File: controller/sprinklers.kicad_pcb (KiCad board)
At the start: 2 copper layers, 155.1 x 162.1 mm, 144 parts, among them J1 Conn_01x02, J2 Conn_01x02, J3 Conn_01x02, J4 Conn_01x02, J5 Conn_01x02, J6 Conn_01x02, K1 SANYOU_SRD_Form_C, K2 SANYOU_SRD_Form_C, K3 SANYOU_SRD_Form_C, K4 SANYOU_SRD_Form_C, K5 SANYOU_SRD_Form_C, K6 SANYOU_SRD_Form_C, Q1 Q_NMOS_GDS, Q2 Q_NMOS_GDS, Q3 Q_NMOS_GDS, Q4 Q_NMOS_GDS, Q5 Q_NMOS_GDS, Q6 Q_NMOS_GDS, U1 LM2596S-5, U2 ESP32-WROOM-32U, U3 AP1117-33

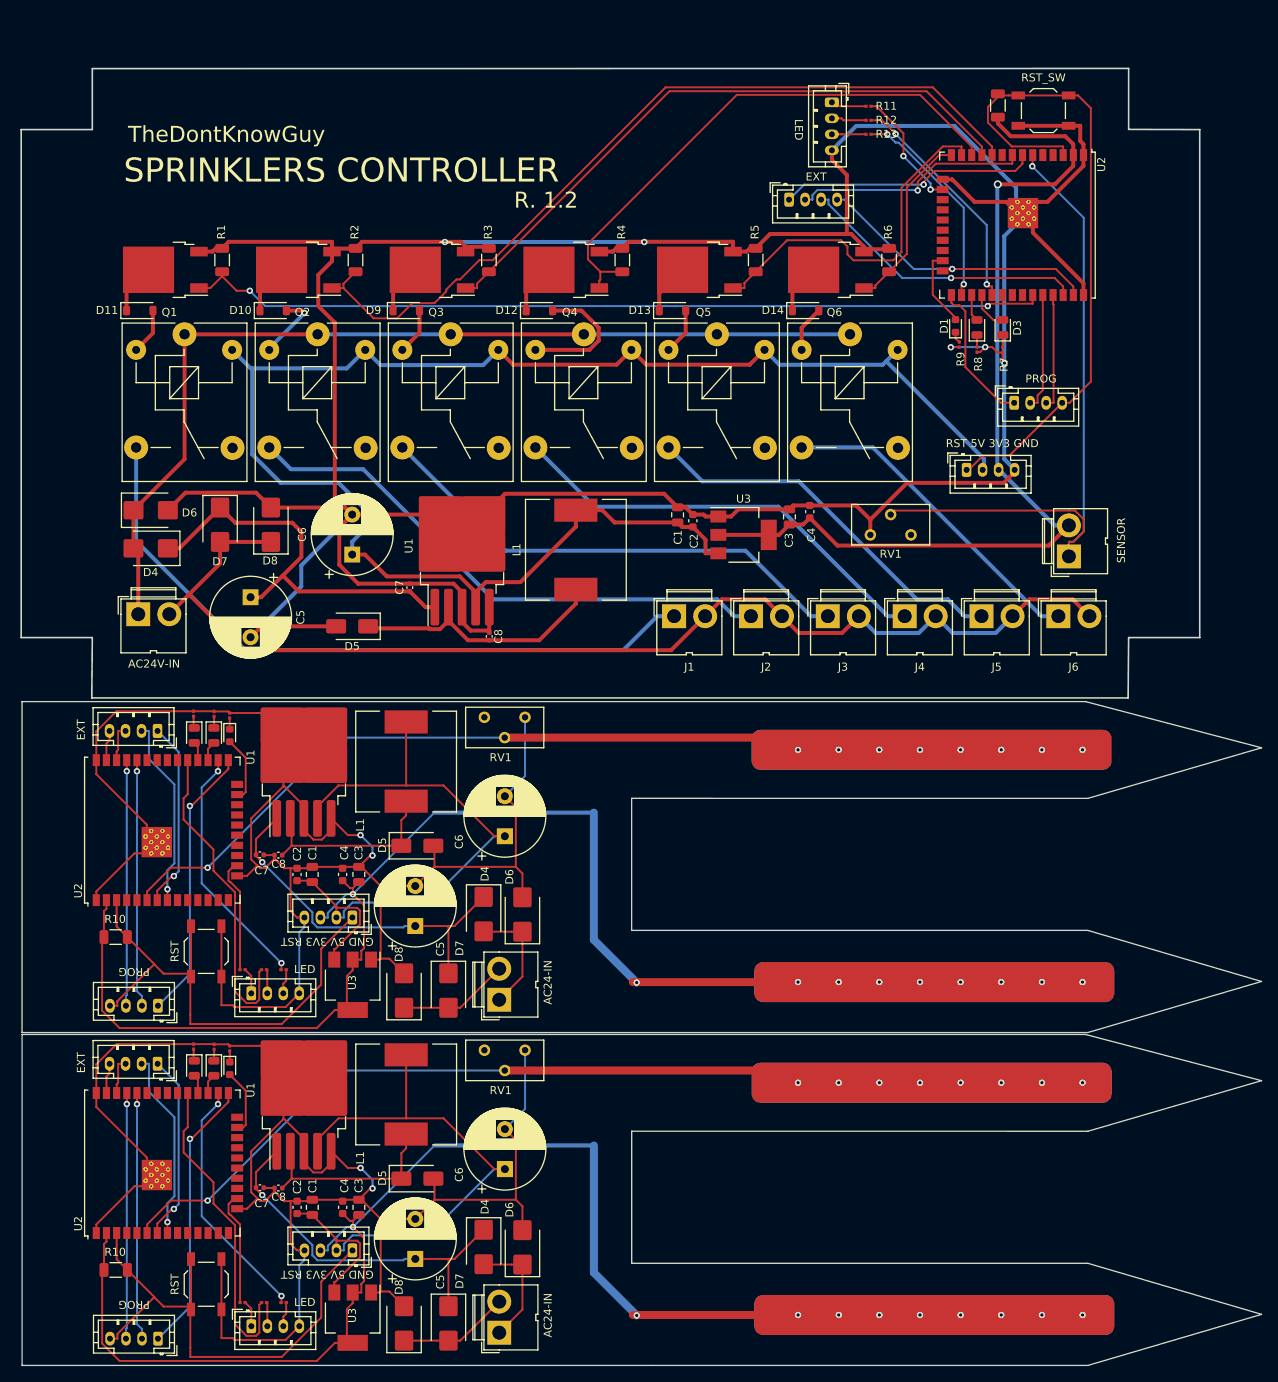
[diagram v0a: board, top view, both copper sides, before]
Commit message: fix footprint
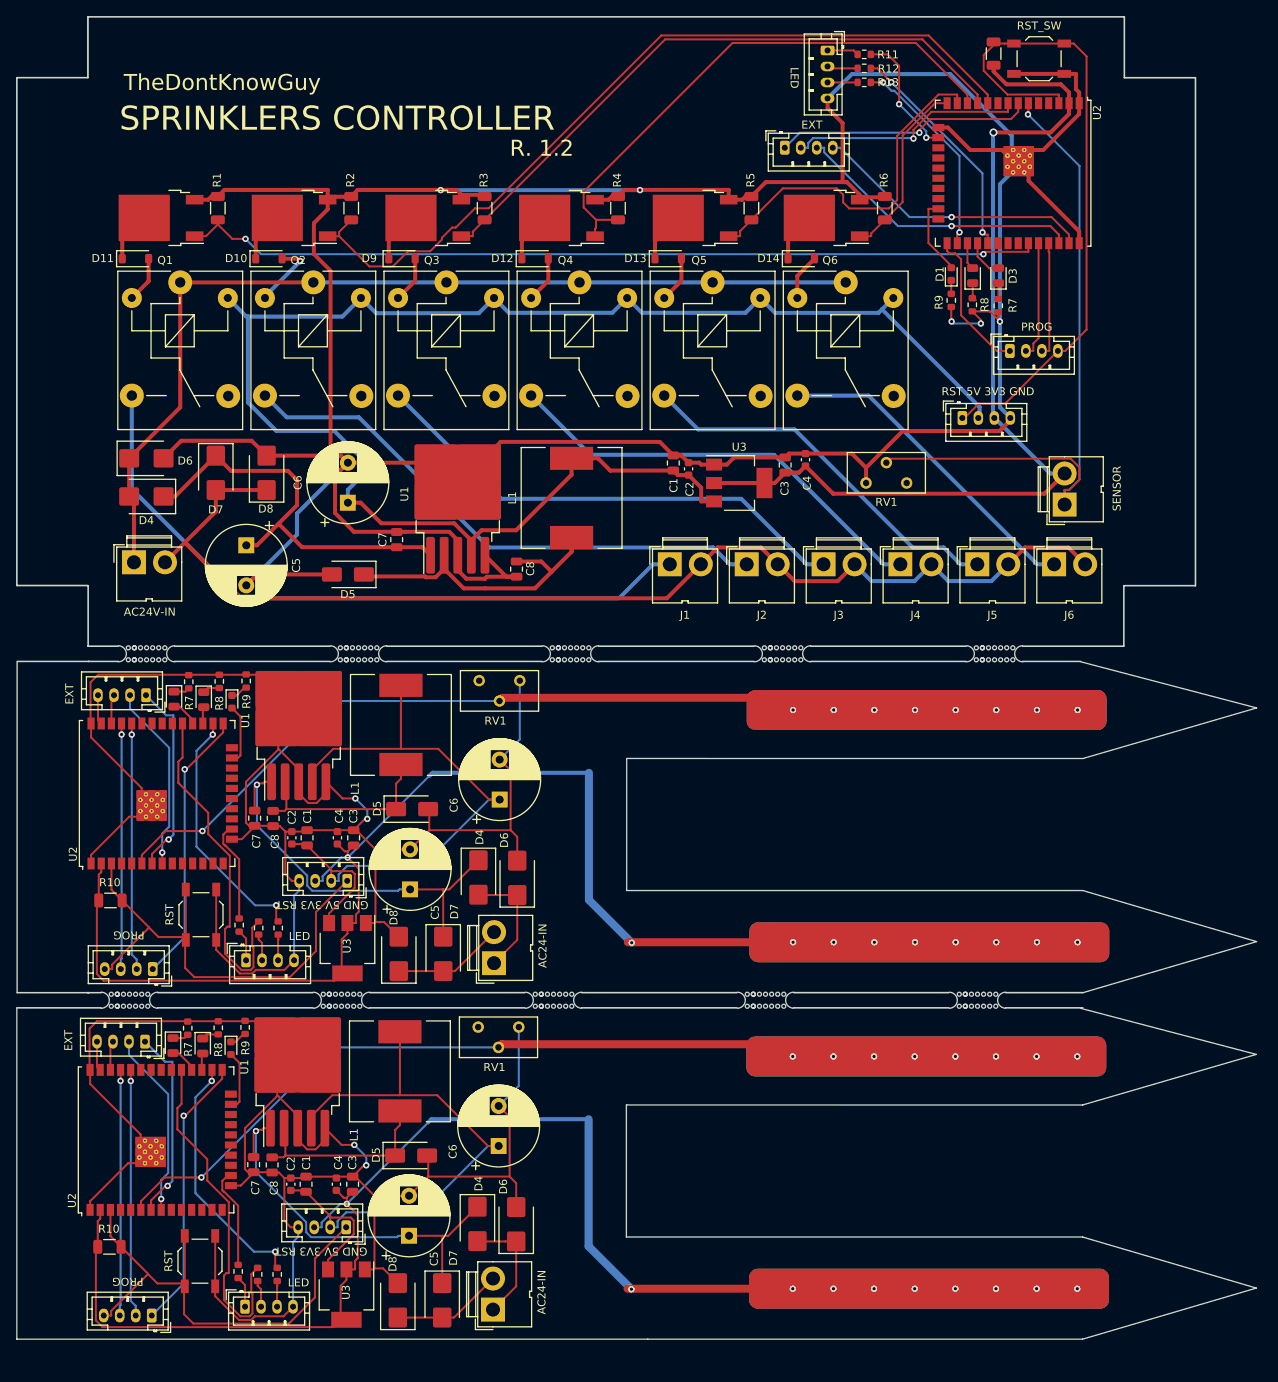
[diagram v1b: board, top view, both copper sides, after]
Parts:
- removed the ? at (129.9, 175.0) (x2)
- removed the ? at (31.8, 162.4)
- removed the ? at (129.6, 145.9) (x2)
- removed the ? at (86.4, 35.6)
- removed the AC24-IN1 at (30.4, 87.4)
- removed the AC24-IN1 at (75.5, 135.6)
- removed the AC24-IN1 at (75.5, 177.2)
- removed the C1 at (52.2, 119.9)
- removed the C1 at (52.2, 161.5)
- removed the C1 at (97.8, 75.0)
- removed the C2 at (99.7, 75.7)
- removed the C2 at (50.3, 119.9)
- removed the C2 at (50.3, 161.5)
- removed the C3 at (111.8, 75.2)
- removed the C3 at (58.0, 119.9)
- removed the C3 at (58.0, 161.5)
- removed the C4 at (56.0, 119.9)
- removed the C4 at (114.3, 74.6)
- removed the C4 at (56.0, 161.5)
- removed the C5 at (44.5, 85.3)
- removed the C5 at (65.0, 126.4)
- removed the C5 at (65.0, 168.0)
- removed the C6 at (57.1, 79.9)
- removed the C6 at (76.2, 115.1)
- removed the C6 at (76.2, 156.7)
- removed the C7 at (45.6, 159.1)
- removed the C7 at (64.4, 84.1)
- removed the C7 at (45.6, 117.5)
- removed the C8 at (47.9, 159.1)
- removed the C8 at (47.9, 117.5)
- removed the C8 at (74.3, 90.2)
- removed the D1 at (132.6, 51.4)
- removed the D1 at (41.8, 102.5)
- removed the D1 at (41.8, 144.1)
- removed the D2 at (135.3, 51.5)
- removed the D2 at (39.9, 144.1)
- removed the D2 at (39.9, 102.5)
- removed the D3 at (138.5, 51.5)
- removed the D3 at (37.4, 102.5)
- removed the D3 at (37.4, 144.1)
- removed the D4 at (73.6, 166.5)
- removed the D4 at (73.6, 124.9)
- removed the D4 at (32.0, 79.2)
- removed the D5 at (65.3, 157.9)
- removed the D5 at (57.1, 88.9)
- removed the D5 at (65.3, 116.3)
- removed the D6 at (32.0, 74.4)
- removed the D6 at (78.4, 124.9)
- removed the D6 at (78.4, 166.5)
- removed the D7 at (69.2, 134.4)
- removed the D7 at (40.6, 76.2)
- removed the D7 at (69.2, 176.0)
- removed the D8 at (63.6, 134.4)
- removed the D8 at (63.6, 176.0)
- removed the D8 at (47.0, 76.2)
- removed the EXT1 at (32.8, 102.0)
- removed the EXT1 at (32.8, 143.6)
- removed the EXT1 at (111.8, 35.6)
- removed the L1 at (63.9, 105.8)
- removed the L1 at (63.9, 147.4)
- removed the L1 at (85.1, 79.3)
- removed the LED1 at (44.5, 176.4)
- removed the LED1 at (117.1, 23.4)
- removed the LED1 at (44.5, 134.8)
- removed the POWER1 at (57.2, 125.3)
- removed the POWER1 at (134.0, 69.3)
- removed the POWER1 at (57.2, 166.9)
- removed the PROG1 at (32.9, 177.9)
- removed the PROG1 at (32.9, 136.3)
- removed the PROG1 at (139.9, 61.0)
- removed the R10 at (27.6, 127.7)
- removed the R10 at (137.9, 23.8)
- removed the R10 at (27.6, 169.4)
- removed the R11 at (43.5, 173.4)
- removed the R11 at (121.7, 23.9)
- removed the R11 at (43.4, 131.8)
- removed the R12 at (46.1, 131.8)
- removed the R12 at (46.1, 173.4)
- removed the R12 at (121.7, 25.6)
- removed the R13 at (48.6, 173.4)
- removed the R13 at (48.6, 131.8)
- removed the R13 at (121.7, 27.4)
- removed the R7 at (37.3, 141.4)
- removed the R7 at (138.5, 54.4)
- removed the R7 at (37.3, 99.8)
- removed the R8 at (39.9, 141.5)
- removed the R8 at (39.9, 99.9)
- removed the R8 at (135.2, 54.3)
- removed the R9 at (133.0, 53.7)
- removed the R9 at (41.8, 141.7)
- removed the R9 at (41.8, 100.1)
- removed the RST_SW1 at (38.9, 171.1)
- removed the RST_SW1 at (143.6, 24.4)
- removed the RST_SW1 at (38.9, 129.5)
- removed the RV1 at (121.9, 77.5)
- removed the RV1 at (78.8, 141.9)
- removed the RV1 at (78.8, 100.3)
- removed the U1 at (70.9, 78.9)
- removed the U1 at (51.1, 146.9)
- removed the U1 at (51.1, 105.3)
- removed the U2 at (33.4, 114.4)
- removed the U2 at (140.3, 38.7)
- removed the U2 at (33.4, 156.0)
- removed the U3 at (106.1, 77.5)
- removed the U3 at (57.2, 175.3)
- removed the U3 at (57.2, 133.7)
- added ? (x2): , , F.Cu at (128.9, 142.7)
- added ?: LOGO, my lib:sprinklers qr code, B.Cu at (85.8, 29.1)
- added ? (x2): , , F.Cu at (129.3, 171.7)
- added ?: LOGO, my lib:sprinklers qr code, B.Cu at (31.7, 163.6)
- added AC24-IN1: Conn_01x02, Connector:JWT_A3963_1x02_P3.96mm_Vertical, F.Cu at (74.8, 174.3)
- added AC24-IN1: Conn_01x02, Connector:JWT_A3963_1x02_P3.96mm_Vertical, F.Cu at (74.9, 131.0)
- added AC24-IN1: Conn_01x02, Connector:JWT_A3963_1x02_P3.96mm_Vertical, F.Cu at (29.9, 80.9)
- added C1: 10uF, Capacitor_SMD:C_0805_2012Metric, F.Cu at (51.4, 158.6)
- added C1: 10uF, Capacitor_SMD:C_0805_2012Metric, F.Cu at (51.5, 115.3)
- added C1: 10uF, Capacitor_SMD:C_0805_2012Metric, F.Cu at (97.3, 68.5)
- added C2: 100nF, Capacitor_SMD:C_0603_1608Metric, F.Cu at (49.6, 115.3)
- added C2: 100nF, Capacitor_SMD:C_0603_1608Metric, F.Cu at (49.5, 158.6)
- added C2: 100nF, Capacitor_SMD:C_0603_1608Metric, F.Cu at (99.2, 69.2)
- added C3: 10uF, Capacitor_SMD:C_0805_2012Metric, F.Cu at (111.3, 68.7)
- added C3: 10uF, Capacitor_SMD:C_0805_2012Metric, F.Cu at (57.3, 115.3)
- added C3: 10uF, Capacitor_SMD:C_0805_2012Metric, F.Cu at (57.2, 158.6)
- added C4: 100nF, Capacitor_SMD:C_0603_1608Metric, F.Cu at (113.8, 68.1)
- added C4: 100nF, Capacitor_SMD:C_0603_1608Metric, F.Cu at (55.3, 115.3)
- added C4: 100nF, Capacitor_SMD:C_0603_1608Metric, F.Cu at (55.2, 158.6)
- added C5: C_Polarized, Capacitor_THT:CP_Radial_D10.0mm_P5.00mm, F.Cu at (64.3, 165.1)
- added C5: C_Polarized, Capacitor_THT:CP_Radial_D10.0mm_P5.00mm, F.Cu at (64.4, 121.8)
- added C5: C_Polarized, Capacitor_THT:CP_Radial_D10.0mm_P5.00mm, F.Cu at (43.9, 78.8)
- added C6: C_Polarized, Capacitor_THT:CP_Radial_D10.0mm_P5.00mm, F.Cu at (75.6, 110.6)
- added C6: C_Polarized, Capacitor_THT:CP_Radial_D10.0mm_P5.00mm, F.Cu at (75.5, 153.9)
- added C6: C_Polarized, Capacitor_THT:CP_Radial_D10.0mm_P5.00mm, F.Cu at (56.6, 73.4)
- added C7: 25V 1uF X5R ±10% 0402 Multilayer Ceramic Capacitors MLCC - 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, Capacitor_SMD:C_0805_2012Metric, F.Cu at (44.8, 156.2)
- added C7: 25V 1uF X5R ±10% 0402 Multilayer Ceramic Capacitors MLCC - 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, Capacitor_SMD:C_0805_2012Metric, F.Cu at (62.7, 78.1)
- added C7: 25V 1uF X5R ±10% 0402 Multilayer Ceramic Capacitors MLCC - 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, Capacitor_SMD:C_0805_2012Metric, F.Cu at (45.0, 112.9)
- added C8: 25V 1uF X5R ±10% 0402 Multilayer Ceramic Capacitors MLCC - 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, Capacitor_SMD:C_0805_2012Metric, F.Cu at (47.3, 112.9)
- added C8: 25V 1uF X5R ±10% 0402 Multilayer Ceramic Capacitors MLCC - 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, Capacitor_SMD:C_0805_2012Metric, F.Cu at (77.7, 81.7)
- added C8: 25V 1uF X5R ±10% 0402 Multilayer Ceramic Capacitors MLCC - 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, Capacitor_SMD:C_0805_2012Metric, F.Cu at (47.1, 156.2)
- added D1: LED, LED_SMD:LED_0603_1608Metric, F.Cu at (132.0, 44.9)
- added D1: LED, LED_SMD:LED_0603_1608Metric, F.Cu at (42.0, 141.6)
- added D1: LED, LED_SMD:LED_0603_1608Metric, F.Cu at (42.1, 98.3)
- added D2: LED, LED_SMD:LED_0805_2012Metric, F.Cu at (38.5, 141.4)
- added D2: LED, LED_SMD:LED_0805_2012Metric, F.Cu at (38.6, 98.1)
- added D2: LED, LED_SMD:LED_0805_2012Metric, F.Cu at (134.7, 45.1)
- added D3: LED, LED_SMD:LED_0805_2012Metric, F.Cu at (137.9, 45.1)
- added D3: LED, LED_SMD:LED_0805_2012Metric, F.Cu at (34.8, 141.3)
- added D3: LED, LED_SMD:LED_0805_2012Metric, F.Cu at (34.9, 98.0)
- added D4: 900mV@2A 30ns 2A 50V DO-214AA Diodes, Diode_SMD:D_SMB, F.Cu at (31.4, 72.7)
- added D4: 900mV@2A 30ns 2A 50V DO-214AA Diodes, Diode_SMD:D_SMB, F.Cu at (72.9, 120.3)
- added D4: 900mV@2A 30ns 2A 50V DO-214AA Diodes, Diode_SMD:D_SMB, F.Cu at (72.8, 163.6)
- added D5: B140-E3, Diode_SMD:D_SMA, F.Cu at (64.6, 111.7)
- added D5: B140-E3, Diode_SMD:D_SMA, F.Cu at (64.5, 155.1)
- added D5: B140-E3, Diode_SMD:D_SMA, F.Cu at (56.6, 82.4)
- added D6: 900mV@2A 30ns 2A 50V DO-214AA Diodes, Diode_SMD:D_SMB, F.Cu at (31.4, 67.9)
- added D6: 900mV@2A 30ns 2A 50V DO-214AA Diodes, Diode_SMD:D_SMB, F.Cu at (77.7, 163.6)
- added D6: 900mV@2A 30ns 2A 50V DO-214AA Diodes, Diode_SMD:D_SMB, F.Cu at (77.8, 120.3)
- added D7: 900mV@2A 30ns 2A 50V DO-214AA Diodes, Diode_SMD:D_SMB, F.Cu at (68.4, 173.1)
- added D7: 900mV@2A 30ns 2A 50V DO-214AA Diodes, Diode_SMD:D_SMB, F.Cu at (68.5, 129.8)
- added D7: 900mV@2A 30ns 2A 50V DO-214AA Diodes, Diode_SMD:D_SMB, F.Cu at (40.1, 69.7)
- added D8: 900mV@2A 30ns 2A 50V DO-214AA Diodes, Diode_SMD:D_SMB, F.Cu at (62.9, 173.1)
- added D8: 900mV@2A 30ns 2A 50V DO-214AA Diodes, Diode_SMD:D_SMB, F.Cu at (46.5, 69.7)
- added D8: 900mV@2A 30ns 2A 50V DO-214AA Diodes, Diode_SMD:D_SMB, F.Cu at (63.0, 129.8)
- added EXT1: Conn_01x04_Pin, Connector_JST:JST_PH_B4B-PH-K_1x04_P2.00mm_Vertical, F.Cu at (31.3, 140.8)
- added EXT1: Conn_01x04_Pin, Connector_JST:JST_PH_B4B-PH-K_1x04_P2.00mm_Vertical, F.Cu at (31.4, 97.5)
- added EXT1: Conn_01x04_Pin, Connector_JST:JST_PH_B4B-PH-K_1x04_P2.00mm_Vertical, F.Cu at (111.2, 29.1)
- added L1: L, Inductor_SMD:L_12x12mm_H8mm, F.Cu at (63.1, 144.5)
- added L1: L, Inductor_SMD:L_12x12mm_H8mm, F.Cu at (84.6, 72.8)
- added L1: L, Inductor_SMD:L_12x12mm_H8mm, F.Cu at (63.2, 101.2)
- added LED1: Conn_01x04_Pin, Connector_JST:JST_PH_B4B-PH-K_1x04_P2.00mm_Vertical, F.Cu at (43.9, 130.6)
- added LED1: Conn_01x04_Pin, Connector_JST:JST_PH_B4B-PH-K_1x04_P2.00mm_Vertical, F.Cu at (43.8, 173.9)
- added LED1: Conn_01x04_Pin, Connector_JST:JST_PH_B4B-PH-K_1x04_P2.00mm_Vertical, F.Cu at (116.6, 16.9)
- added POWER1: Conn_01x04_Pin, Connector_JST:JST_PH_B4B-PH-K_1x04_P2.00mm_Vertical, F.Cu at (56.4, 164.0)
- added POWER1: Conn_01x04_Pin, Connector_JST:JST_PH_B4B-PH-K_1x04_P2.00mm_Vertical, F.Cu at (133.4, 62.9)
- added POWER1: Conn_01x04_Pin, Connector_JST:JST_PH_B4B-PH-K_1x04_P2.00mm_Vertical, F.Cu at (56.5, 120.7)
- added PROG1: Conn_01x04_Pin, Connector_JST:JST_PH_B4B-PH-K_1x04_P2.00mm_Vertical, F.Cu at (32.2, 131.7)
- added PROG1: Conn_01x04_Pin, Connector_JST:JST_PH_B4B-PH-K_1x04_P2.00mm_Vertical, F.Cu at (139.4, 54.5)
- added PROG1: Conn_01x04_Pin, Connector_JST:JST_PH_B4B-PH-K_1x04_P2.00mm_Vertical, F.Cu at (32.1, 175.0)
- added R10: 10K, Resistor_SMD:R_1206_3216Metric, F.Cu at (26.9, 123.2)
- added R10: 10K, Resistor_SMD:R_1206_3216Metric, F.Cu at (26.8, 166.5)
- added R10: 10K, Resistor_SMD:R_1206_3216Metric, F.Cu at (137.3, 17.3)
- added R11: 130, Resistor_SMD:R_0603_1608Metric, F.Cu at (121.2, 17.4)
- added R11: 130, Resistor_SMD:R_0603_1608Metric, F.Cu at (43.0, 126.2)
- added R11: 130, Resistor_SMD:R_0603_1608Metric, F.Cu at (42.9, 169.5)
- added R12: 130, Resistor_SMD:R_0603_1608Metric, F.Cu at (45.3, 169.9)
- added R12: 130, Resistor_SMD:R_0603_1608Metric, F.Cu at (45.5, 126.6)
- added R12: 130, Resistor_SMD:R_0603_1608Metric, F.Cu at (121.2, 19.2)
- added R13: 130, Resistor_SMD:R_0603_1608Metric, F.Cu at (47.9, 126.6)
- added R13: 130, Resistor_SMD:R_0603_1608Metric, F.Cu at (47.8, 169.9)
- added R13: 130, Resistor_SMD:R_0603_1608Metric, F.Cu at (121.2, 20.9)
- added R7: 130, Resistor_SMD:R_0603_1608Metric, F.Cu at (36.6, 139.1)
- added R7: 130, Resistor_SMD:R_0603_1608Metric, F.Cu at (137.9, 48.8)
- added R7: 130, Resistor_SMD:R_0603_1608Metric, F.Cu at (36.7, 95.8)
- added R8: 130, Resistor_SMD:R_0603_1608Metric, F.Cu at (40.5, 95.8)
- added R8: 130, Resistor_SMD:R_0603_1608Metric, F.Cu at (134.7, 48.7)
- added R8: 130, Resistor_SMD:R_0603_1608Metric, F.Cu at (40.4, 139.1)
- added R9: 130, Resistor_SMD:R_0603_1608Metric, F.Cu at (43.8, 139.0)
- added R9: 130, Resistor_SMD:R_0603_1608Metric, F.Cu at (43.9, 95.7)
- added R9: 130, Resistor_SMD:R_0603_1608Metric, F.Cu at (132.0, 48.2)
- added RST_SW1: SW_SPST, Button_Switch_SMD:SW_SPST_TL3342, F.Cu at (38.3, 125.0)
- added RST_SW1: SW_SPST, Button_Switch_SMD:SW_SPST_TL3342, F.Cu at (38.1, 168.3)
- added RST_SW1: SW_SPST, Button_Switch_SMD:SW_SPST_TL3342, F.Cu at (143.0, 17.9)
- added RV1: R_Potentiometer_Small, Potentiometer_THT:Potentiometer_Bourns_3296Y_Vertical, F.Cu at (78.0, 139.0)
- added RV1: R_Potentiometer_Small, Potentiometer_THT:Potentiometer_Bourns_3296Y_Vertical, F.Cu at (121.4, 71.0)
- added RV1: R_Potentiometer_Small, Potentiometer_THT:Potentiometer_Bourns_3296Y_Vertical, F.Cu at (78.1, 95.7)
- added U1: LM2596S-5, Package_TO_SOT_SMD:TO-263-5_TabPin3, F.Cu at (50.5, 100.7)
- added U1: LM2596S-5, Package_TO_SOT_SMD:TO-263-5_TabPin3, F.Cu at (50.3, 144.0)
- added U1: LM2596S-5, Package_TO_SOT_SMD:TO-263-5_TabPin3, F.Cu at (70.3, 72.4)
- added U2: ESP32-WROOM-32U, RF_Module:ESP32-WROOM-32U, F.Cu at (32.6, 153.1)
- added U2: ESP32-WROOM-32U, RF_Module:ESP32-WROOM-32U, F.Cu at (139.8, 32.3)
- added U2: ESP32-WROOM-32U, RF_Module:ESP32-WROOM-32U, F.Cu at (32.8, 109.8)
- added U3: AP1117-33, Package_TO_SOT_SMD:SOT-223-3_TabPin2, F.Cu at (105.5, 71.0)
- added U3: AP1117-33, Package_TO_SOT_SMD:SOT-223-3_TabPin2, F.Cu at (56.6, 129.1)
- added U3: AP1117-33, Package_TO_SOT_SMD:SOT-223-3_TabPin2, F.Cu at (56.4, 172.4)
- added mouse-bite-2mm-slot: VAL**, Mouse Bites:mouse-bite-2mm-slot, F.Cu at (29.9, 92.3)
- added mouse-bite-2mm-slot: VAL**, Mouse Bites:mouse-bite-2mm-slot, F.Cu at (27.8, 135.6)
- added mouse-bite-2mm-slot5: VAL**, Mouse Bites:mouse-bite-2mm-slot, F.Cu at (56.4, 92.3)
- added mouse-bite-2mm-slot5: VAL**, Mouse Bites:mouse-bite-2mm-slot, F.Cu at (54.3, 135.6)
- added mouse-bite-2mm-slot6: VAL**, Mouse Bites:mouse-bite-2mm-slot, F.Cu at (80.8, 135.6)
- added mouse-bite-2mm-slot6: VAL**, Mouse Bites:mouse-bite-2mm-slot, F.Cu at (82.9, 92.3)
- added mouse-bite-2mm-slot7: VAL**, Mouse Bites:mouse-bite-2mm-slot, F.Cu at (109.4, 92.3)
- added mouse-bite-2mm-slot7: VAL**, Mouse Bites:mouse-bite-2mm-slot, F.Cu at (107.3, 135.6)
- added mouse-bite-2mm-slot8: VAL**, Mouse Bites:mouse-bite-2mm-slot, F.Cu at (135.9, 92.3)
- added mouse-bite-2mm-slot8: VAL**, Mouse Bites:mouse-bite-2mm-slot, F.Cu at (133.8, 135.6)
- moved SENSOR1 6.51 mm to (146.2, 73.7)
- moved R3 6.51 mm to (73.7, 36.6)
- moved R4 6.51 mm to (90.4, 36.6)
- moved R6 6.51 mm to (123.7, 36.6)
- moved R1 6.51 mm to (40.4, 36.6)
- moved R2 6.51 mm to (57.0, 36.6)
- moved R5 6.51 mm to (107.1, 36.6)
- moved D10 6.51 mm to (46.7, 42.9)
- moved D12 6.51 mm to (80.0, 42.9)
- moved D13 6.51 mm to (96.7, 42.9)
- moved D14 6.51 mm to (113.3, 42.9)
- moved D9 6.51 mm to (63.4, 42.9)
- moved J1 6.51 mm to (96.9, 81.1)
- moved J5 6.51 mm to (135.3, 81.1)
- moved J6 6.51 mm to (144.9, 81.1)
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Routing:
- net Net-(D12-A): track 16.6 -> 5.80 mm
- net Net-(D4-K): track 144.6 -> 151.7 mm
- net Net-(U2-IO5): track 108.1 -> 114.1 mm
- net Net-(D5-K): track 82.3 -> 87.4 mm
- net Net-(POWER1-Pin_1): track 210.2 -> 205.7 mm
- net Net-(U2-IO13): track 44.2 -> 41.6 mm
- net Net-(D3-A): track 9.57 -> 11.9 mm
- net GRD: track 937.0 -> 939.1 mm
- net Net-(EXT1-Pin_3): track 45.5 -> 43.5 mm
- net Net-(D2-K): track 4.38 -> 6.21 mm
- net 3V3: track 418.5 -> 416.7 mm
- net Net-(D3-K): track 4.52 -> 6.05 mm
- net Net-(LED1-Pin_1): track 11.0 -> 12.5 mm
- net Net-(D1-A): track 26.2 -> 24.7 mm
- net Net-(EXT1-Pin_1): track 79.3 -> 80.8 mm
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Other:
- board size 155.1 x 162.1 mm -> 155 x 165.3 mm
- board text removed: "<-- V-CUT"
